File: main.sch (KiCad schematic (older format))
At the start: 7 parts, among them J301 Conn_01x14, J302 Conn_01x09, J303 Conn_02x05_Odd_Even, U503 TL074

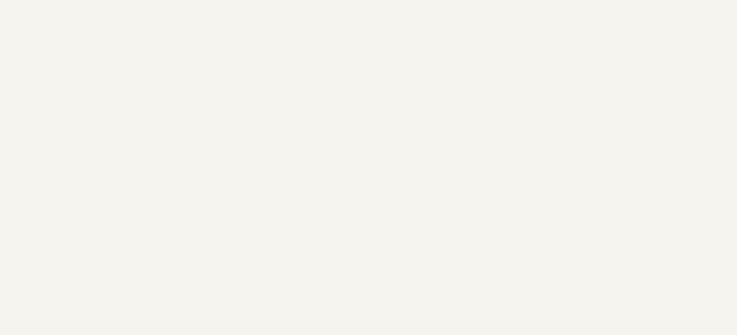
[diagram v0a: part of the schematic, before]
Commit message: Fixed op amp issue
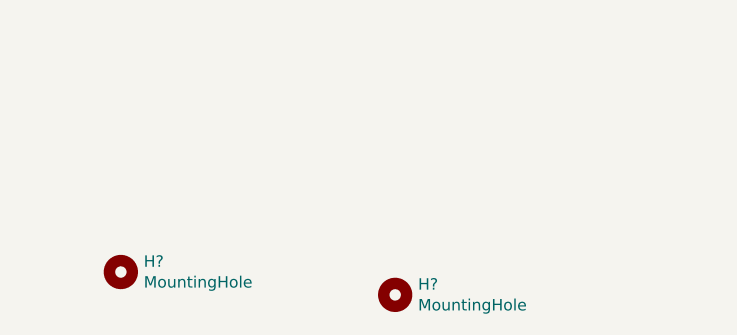
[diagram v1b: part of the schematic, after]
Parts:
- added H? (x2): MountingHole, MountingHole:MountingHole_3mm_Pad, symbol Mechanical:MountingHole
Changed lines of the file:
@@
 Wire Wire Line
 	8150 2100 7400 2100
+$Comp
+L Mechanical:MountingHole H?
+U 1 1 60AFB2FA
+P 1800 5150
+F 0 "H?" H 1900 5196 50  0000 L CNN
+F 1 "MountingHole" H 1900 5105 50  0000 L CNN
+F 2 "MountingHole:MountingHole_3mm_Pad" H 1800 5150 50  0001 C CNN
+F 3 "~" H 1800 5150 50  0001 C CNN
+	1    1800 5150
+	1    0    0    -1
+$EndComp
+$Comp
+L Mechanical:MountingHole H?
+U 1 1 60AFF86F
+P 3000 5250
+F 0 "H?" H 3100 5296 50  0000 L CNN
+F 1 "MountingHole" H 3100 5205 50  0000 L CNN
+F 2 "MountingHole:MountingHole_3mm_Pad" H 3000 5250 50  0001 C CNN
+F 3 "~" H 3000 5250 50  0001 C CNN
+	1    3000 5250
+	1    0    0    -1
+$EndComp
 $EndSCHEMATC
